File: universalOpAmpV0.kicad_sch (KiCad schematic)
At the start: 11 parts, among them J1 BNC I1, J2 BNC I2, J3 BNC I3, J4 BNC O1, J5 BNC O2, J6 BNC O3, SW13 SW_DIP_x08, SW14 SW_DIP_x08, SW15 SW_DIP_x08, SW60 SW_Coded_SH-7080

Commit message: minor schematic changes, 4 way dip now used instead of 6. switch and pot footprints and symbols done
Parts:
- removed SW13, SW14, SW15: SW_DIP_x08, symbol Switch:SW_DIP_x08
- added SW1: 218-8LPSTR, symbol uniOpAmpLib:218-8LPSTR
- renumbered RN2 to RN1, SW60 to SW4
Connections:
- net N1: now also SW1.16
- net N2: now also SW1.15
- net N4: now also SW1.14
- net N5: now also SW1.13
- net P1: now also SW1.12
- net P2: now also SW1.11
- net P4: now also SW1.10
- net P5: now also SW1.9
- net at J1.1 (In): now also SW1.1, SW1.2, SW1.3, SW1.4, SW1.5, SW1.6, SW1.7, SW1.8
- net OutputStage2/O: no longer names the net of J5.1 (In)
- net OutputStage3/O: no longer names the net of J6.1 (In)
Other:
- removed sheet OpAmpBlock2
- removed sheet OpAmpBlock3
- removed sheet OpAmpBlock4
- removed sheet OpAmpBlock5
- removed sheet OpAmpBlock6
- removed sheet OutputStage2
- removed sheet OutputStage3

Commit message: Initial PCB layout
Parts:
- renumbered SW4 to SW2
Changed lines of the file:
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@@
 		(dnp no)
 		(fields_autoplaced yes)
-		(property "Reference" "SW4"
+		(property "Reference" "SW2"
 			(at 167.64 151.1299 90)
 			(show_name no)
@@
 			(project "universalOpAmpV0"
 				(path "/0c9d5097-e341-4aa8-a29f-4bc5e653f52f"
-					(reference "SW4")
+					(reference "SW2")
 					(unit 1)
 				)

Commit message: oops scope creep - now there is a frequency counter
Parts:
- removed SW1: 218-8LPSTR, symbol uniOpAmpLib:218-8LPSTR
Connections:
- net InputStage1/I: now reaches J1.1 (In)
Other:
- added sheet FrequencyCounter (FrequencyCounter.kicad_sch)
- added sheet InputStage1 (InputStage.kicad_sch)
- added sheet VoltageSources (VoltageSources.kicad_sch)
- note added: "Summing Amplifier Module (Excluded From Board at the moment) modify dashed rectangle properties to fix"
- note removed: "Summing Amplifier Module"

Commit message: preliminary layout of op amp blocks complete
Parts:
- J1: footprint (none) -> uniOpAmpLib:BNC-0731000105
- J2: value BNC I2 -> BNC I1; footprint (none) -> uniOpAmpLib:BNC-0731000105
- J3: value BNC I3 -> BNC I1; footprint (none) -> uniOpAmpLib:BNC-0731000105
- J4: value BNC O1 -> BNC I1; footprint (none) -> uniOpAmpLib:BNC-0731000105
- J5: value BNC O2 -> BNC I1; footprint (none) -> uniOpAmpLib:BNC-0731000105
- J6: value BNC O3 -> BNC I1; footprint (none) -> uniOpAmpLib:BNC-0731000105
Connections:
- net InputStage3/I: now reaches J3.1 (In)
- net InputStage2/I: now reaches J2.1 (In)
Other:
- added sheet InputStage2 (InputStage.kicad_sch)
- added sheet InputStage3 (InputStage.kicad_sch)
- added sheet OpAmpBlock2 (OpAmpBlock.kicad_sch)
- added sheet OpAmpBlock3 (OpAmpBlock.kicad_sch)
- added sheet OpAmpBlock4 (OpAmpBlock.kicad_sch)
- added sheet OpAmpBlock5 (OpAmpBlock.kicad_sch)
- added sheet OpAmpBlock6 (OpAmpBlock.kicad_sch)
- note added: "Dumbass, just use a 4 or (wait for it) 6 way spst dip switch"

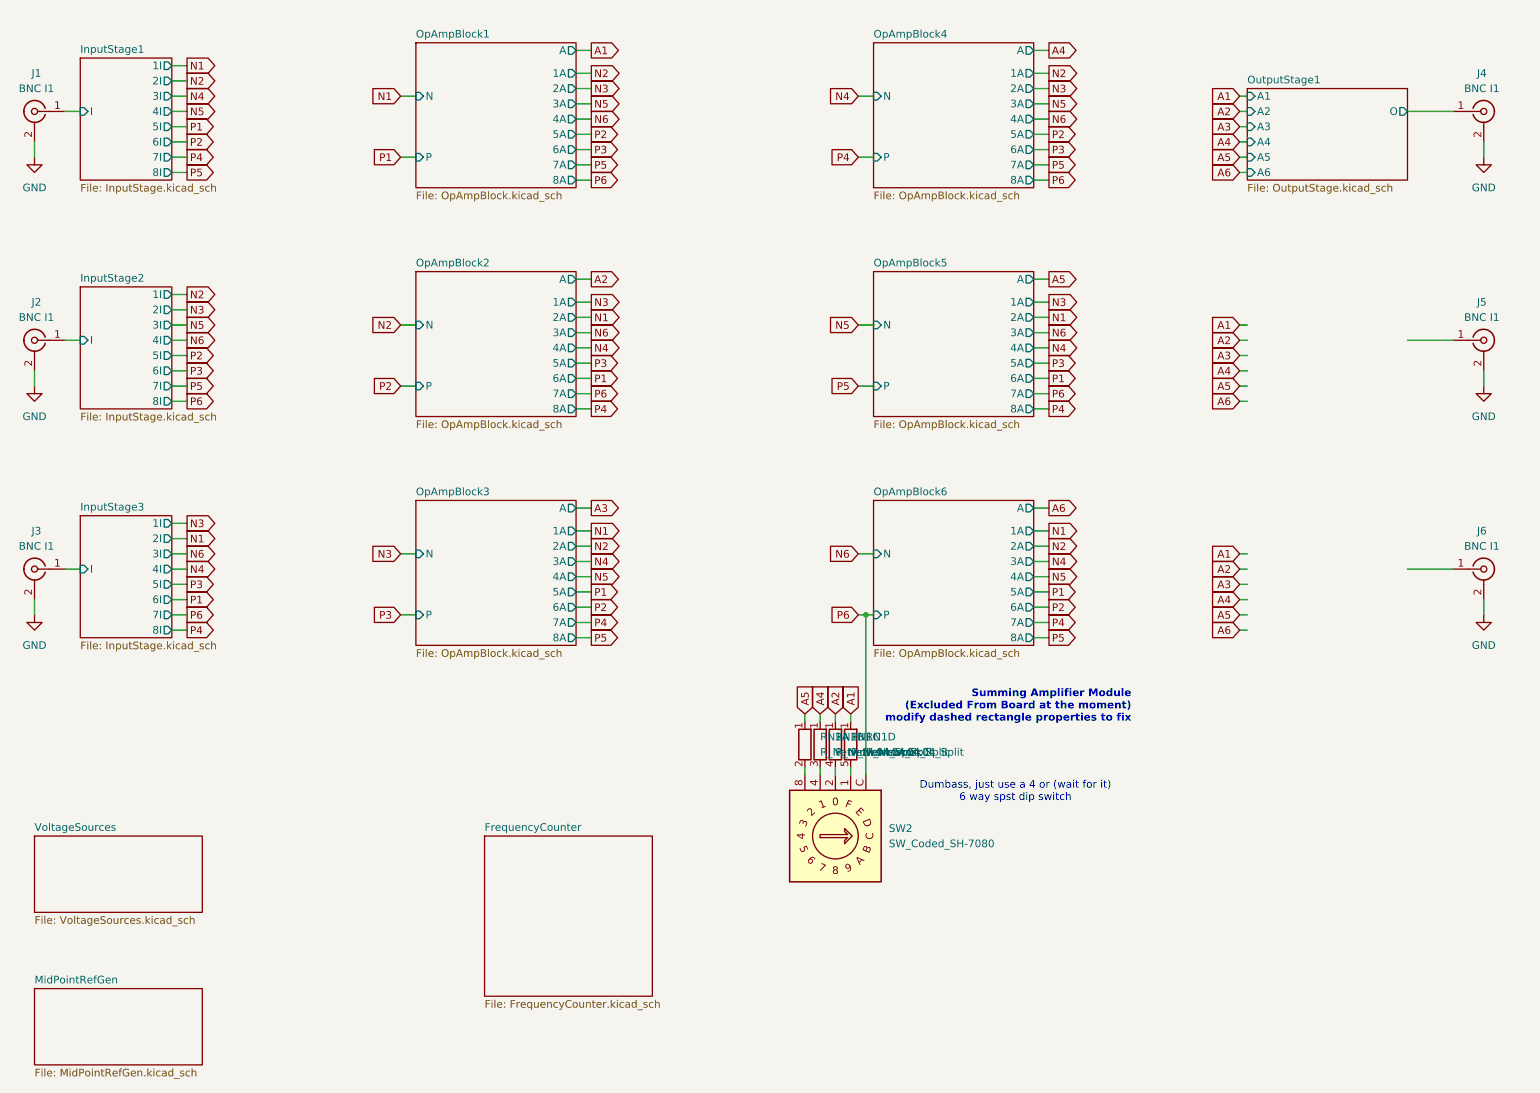
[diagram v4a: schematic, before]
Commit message: initial interconnect bus layout complete, board changed to 6 layers due to bus layer requirements
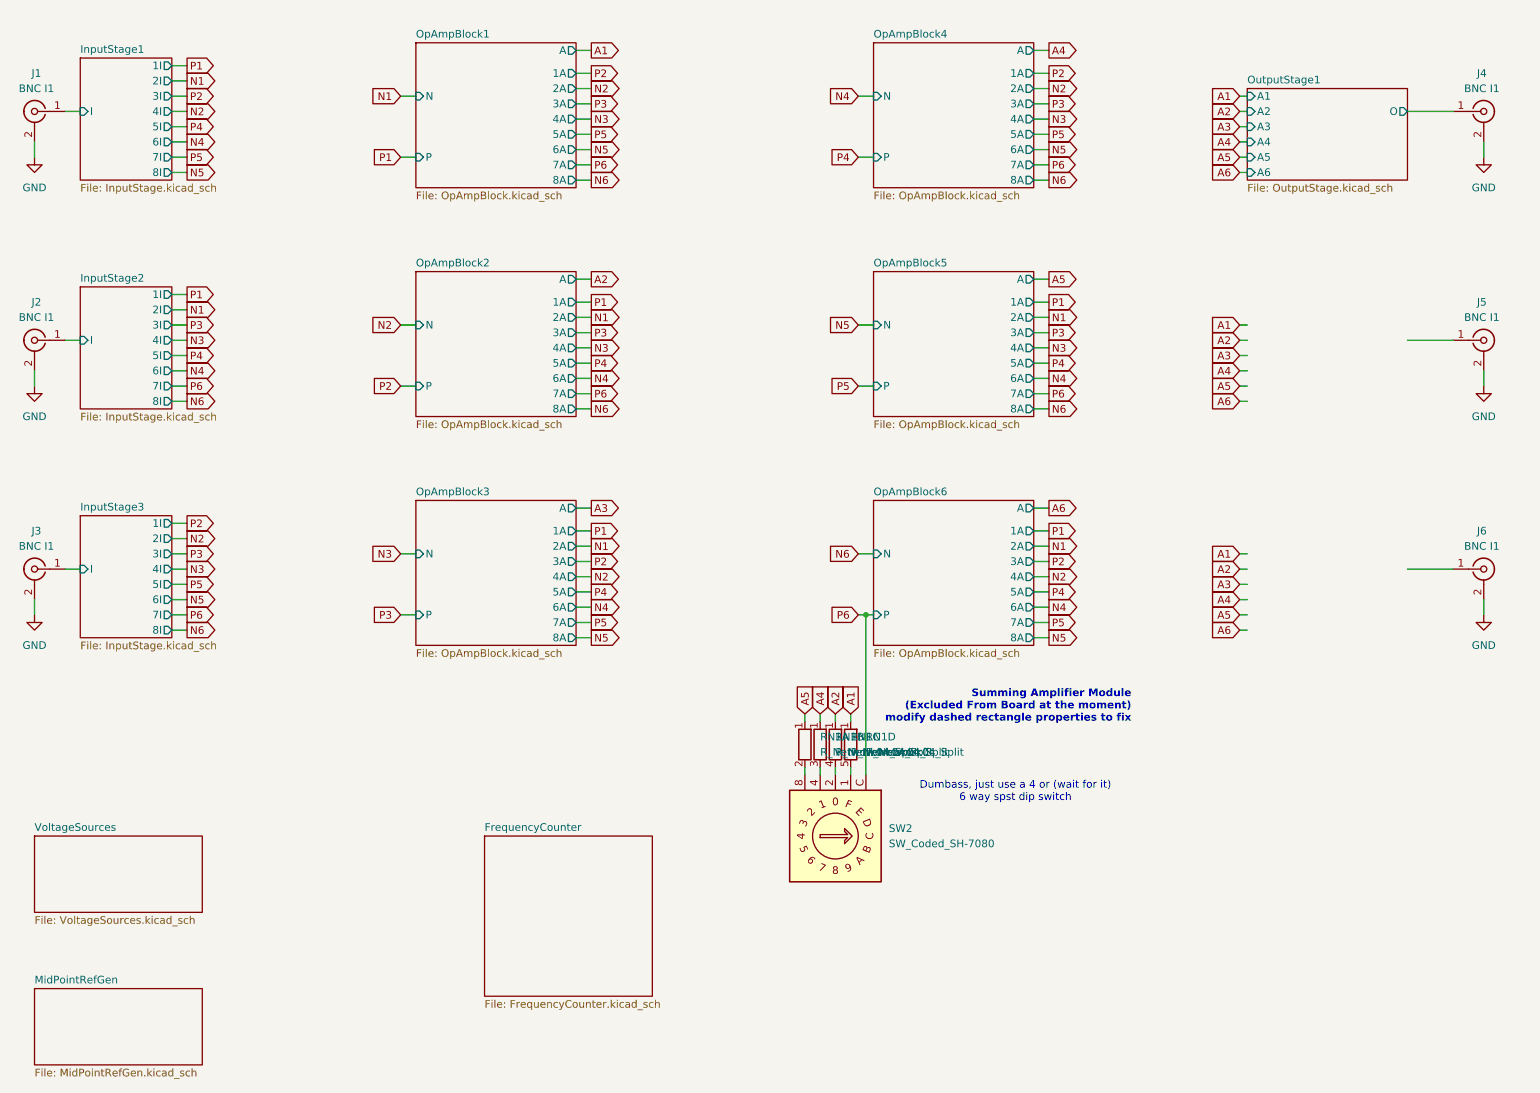
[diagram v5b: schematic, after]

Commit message: Input and output routing complete
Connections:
- net OutputStage3/O: now reaches J6.1 (In)
- net OutputStage2/O: now reaches J5.1 (In)
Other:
- added sheet OutputStage2 (OutputStage.kicad_sch)
- added sheet OutputStage3 (OutputStage.kicad_sch)
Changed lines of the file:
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@@
+	)
+	(sheet
+		(at 227.33 66.04)
+		(size 26.67 15.24)
+		(exclude_from_sim no)
+		(in_bom yes)
+		(on_board yes)
+		(dnp no)
+		(fields_autoplaced yes)
+		(stroke
+			(width 0.1524)
+			(type solid)
+		)
+		(fill
+			(color 0 0 0 0)
+		)
+		(property "Sheetname" "OutputStage2"
+			(at 227.33 65.3284 0)
+			(show_name no)
+			(do_not_autoplace no)
+			(effects
+				(font
+					(size 1.27 1.27)
+				)
+				(justify left bottom)
+			)
+		)
+		(property "Sheetfile" "OutputStage.kicad_sch"
+			(at 227.33 81.8646 0)
+			(show_name no)
+			(do_not_autoplace no)
+			(effects
+				(font
+					(size 1.27 1.27)
+				)
+				(justify left top)
+			)
+		)
+		(pin "A1" input
+			(at 227.33 67.31 180)
+			(effects
+				(font
+					(size 1.27 1.27)
+				)
+				(justify left)
+			)
+		)
+		(pin "A2" input
+			(at 227.33 69.85 180)
+			(effects
+				(font
+					(size 1.27 1.27)
+				)
+				(justify left)
+			)
+		)
+		(pin "A3" input
+			(at 227.33 72.39 180)
+			(effects
+				(font
+					(size 1.27 1.27)
+				)
+				(justify left)
+			)
+		)
+		(pin "A4" input
+			(at 227.33 74.93 180)
+			(effects
+				(font
+					(size 1.27 1.27)
+				)
+				(justify left)
+			)
+		)
+		(pin "A5" input
+			(at 227.33 77.47 180)
+			(effects
+				(font
+					(size 1.27 1.27)
+				)
+				(justify left)
+			)
+		)
+		(pin "A6" input
+			(at 227.33 80.01 180)
+			(effects
+				(font
+					(size 1.27 1.27)
+				)
+				(justify left)
+			)
+		)
+		(pin "O" output
+			(at 254 69.85 0)
+			(effects
+				(font
+					(size 1.27 1.27)
+				)
+				(justify right)
+			)
+		)
+		(instances
+			(project "universalOpAmpV0"
+				(path "/0c9d5097-e341-4aa8-a29f-4bc5e653f52f"
+					(page "15")
+				)
+			)
+		)
 	)
 	(sheet
@@
 				)
 			)
+		)
+	)
+	(sheet
+		(at 227.33 104.14)
+		(size 26.67 15.24)
+		(exclude_from_sim no)
+		(in_bom yes)
+		(on_board yes)
+		(dnp no)
+		(fields_autoplaced yes)
+		(stroke
+			(width 0.1524)
+			(type solid)
+		)
+		(fill
+			(color 0 0 0 0)
+		)
+		(property "Sheetname" "OutputStage3"
+			(at 227.33 103.4284 0)
+			(show_name no)
+			(do_not_autoplace no)
+			(effects
+				(font
+					(size 1.27 1.27)
+				)
+				(justify left bottom)
+			)
+		)
+		(property "Sheetfile" "OutputStage.kicad_sch"
+			(at 227.33 119.9646 0)
+			(show_name no)
+			(do_not_autoplace no)
+			(effects
+				(font
+					(size 1.27 1.27)
+				)
+				(justify left top)
+			)
+		)
+		(pin "A1" input
+			(at 227.33 105.41 180)
+			(effects
+				(font
+					(size 1.27 1.27)
+				)
+				(justify left)
+			)
+		)
+		(pin "A2" input
+			(at 227.33 107.95 180)
+			(effects
+				(font
+					(size 1.27 1.27)
+				)
+				(justify left)
+			)
+		)
+		(pin "A3" input
+			(at 227.33 110.49 180)
+			(effects
+				(font
+					(size 1.27 1.27)
+				)
+				(justify left)
+			)
+		)
+		(pin "A4" input
+			(at 227.33 113.03 180)
+			(effects
+				(font
+					(size 1.27 1.27)
+				)
+				(justify left)
+			)
+		)
+		(pin "A5" input
+			(at 227.33 115.57 180)
+			(effects
+				(font
+					(size 1.27 1.27)
+				)
+				(justify left)
+			)
+		)
+		(pin "A6" input
+			(at 227.33 118.11 180)
+			(effects
+				(font
+					(size 1.27 1.27)
+				)
+				(justify left)
+			)
+		)
+		(pin "O" output
+			(at 254 107.95 0)
+			(effects
+				(font
+					(size 1.27 1.27)
+				)
+				(justify right)
+			)
+		)
+		(instances
+			(project "universalOpAmpV0"
+				(path "/0c9d5097-e341-4aa8-a29f-4bc5e653f52f"
+					(page "16")
+				)
+			)

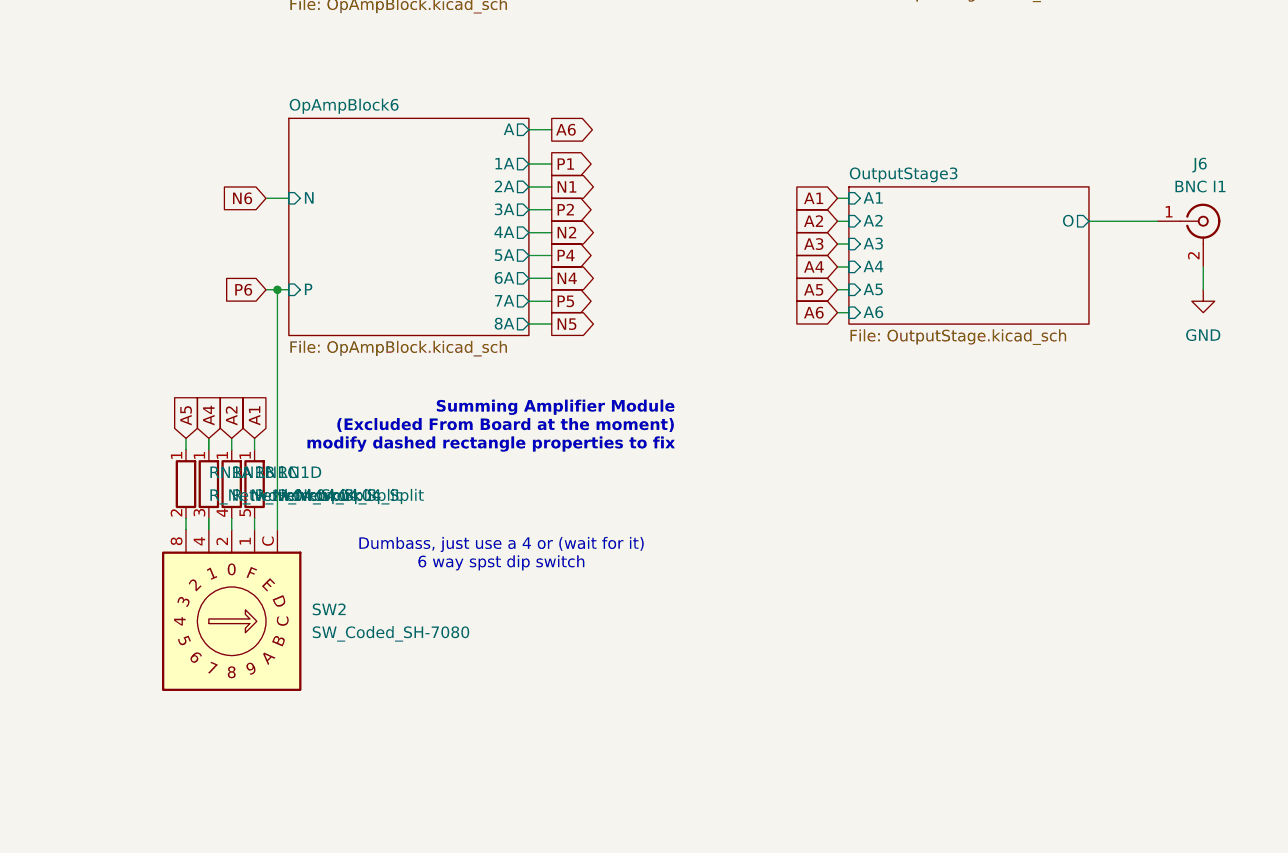
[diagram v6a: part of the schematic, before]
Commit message: Voltage controlled current output circuit and preliminary layout added
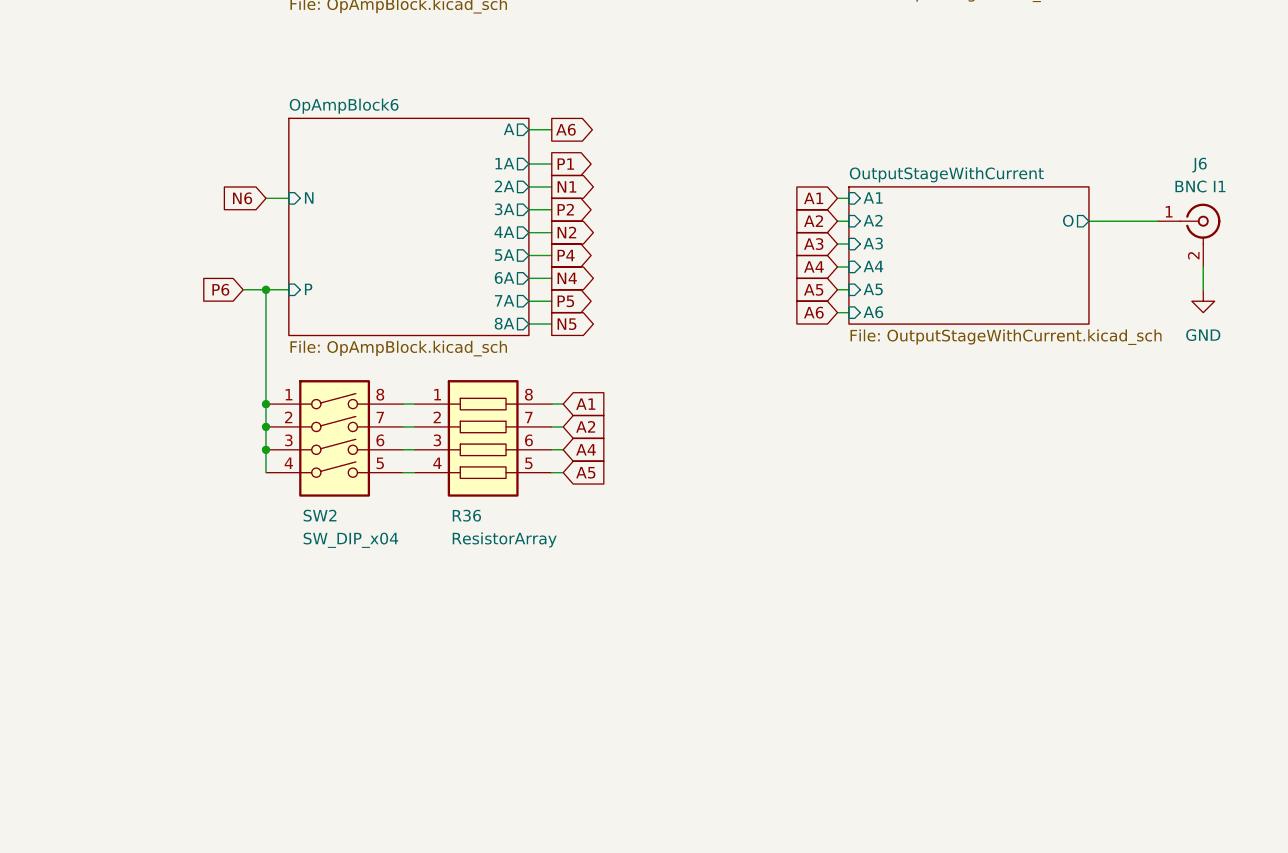
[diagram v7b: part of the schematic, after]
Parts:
- removed RN1: R_Network04_Split, Resistor_THT:R_Array_SIP5, symbol Device:R_Network04_Split
- removed SW2: SW_Coded_SH-7080, Button_Switch_SMD:Nidec_Copal_SH-7040B, symbol Switch:SW_Coded_SH-7080
- added R36: ResistorArray, Resistor_SMD:R_Array_Convex_4x1206, symbol uniOpAmpLib:ResistorArray
- added SW2: SW_DIP_x04, uniOpAmpLib:218-4LPSTR, symbol Switch:SW_DIP_x04
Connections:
- net A1: now also R36.8
- net A2: now also R36.7
- net A4: now also R36.6
- net A5: now also R36.5
- net P6: now also SW2.1, SW2.2, SW2.3, SW2.4
- net OutputStage3/O renamed OutputStageWithCurrent/O
- new net: R36.4, SW2.5
- new net: R36.3, SW2.6
- new net: R36.2, SW2.7
- new net: R36.1, SW2.8
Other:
- removed sheet OutputStage3
- added sheet OutputStageWithCurrent (OutputStageWithCurrent.kicad_sch)
- note removed: "Dumbass, just use a 4 or (wait for it) 6 way spst dip switch"
- note removed: "Summing Amplifier Module (Excluded From Board at the moment) modify dashed rectangle properties to fix"
